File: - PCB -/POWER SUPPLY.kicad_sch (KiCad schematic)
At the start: 5 parts, among them IC1 XT30U-F, U11 LD1086V33-DG, U7 ROB-14450

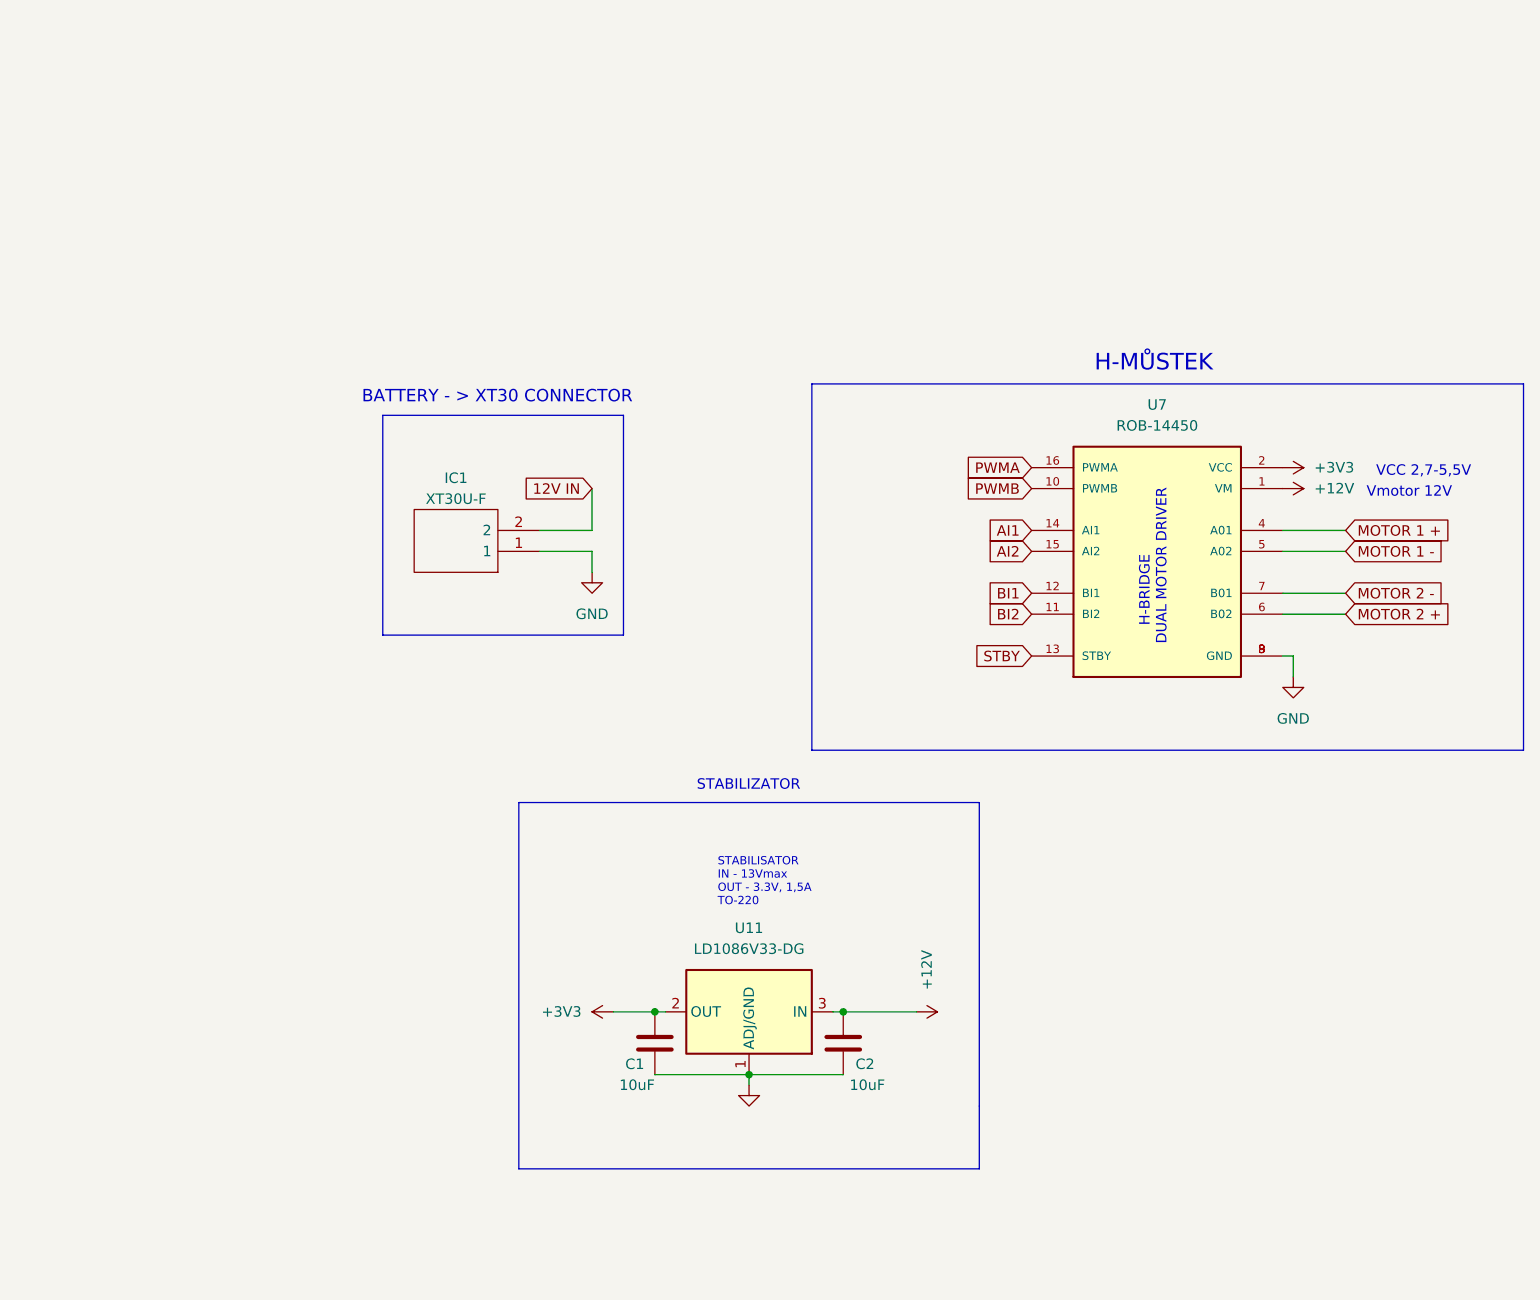
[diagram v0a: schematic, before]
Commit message: PCB - SCH UPDATE (fully labelled and described)
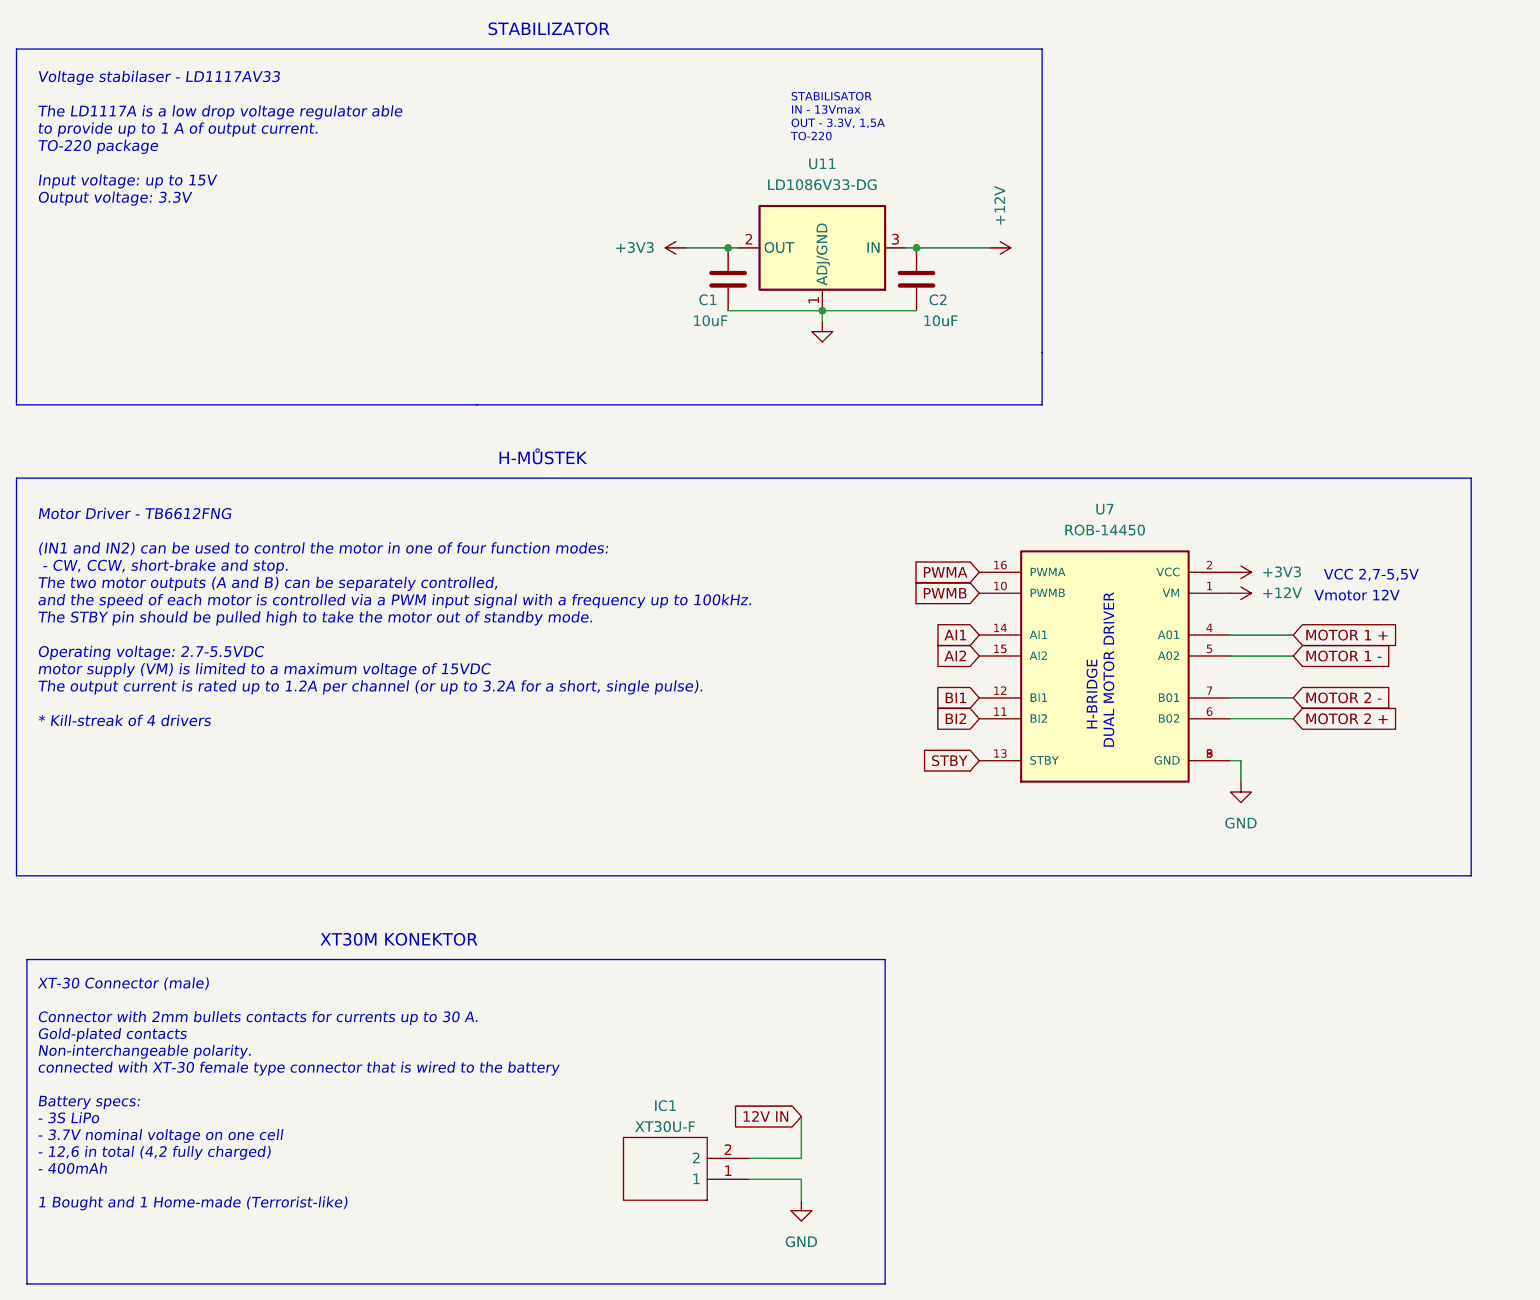
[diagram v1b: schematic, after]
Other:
- note added: "Motor Driver - TB6612FNG (IN1 and IN2) can be used to control the motor in one of four function modes: - CW, CCW, short-brake and stop. The two motor outputs (A and B) can be separately controlled, and the speed of each motor is controlled via a PWM input signal with a frequency up to 100kHz. The STBY pin should be pulled high to take the motor out of standby mode. Operating voltage: 2.7-5.5VDC m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"
- note added: "Voltage stabilaser - LD1117AV33 The LD1117A is a low drop voltage regulator able to provide up to 1 A of output current. TO-220 package Input voltage: up to 15V Output voltage: 3.3V"
- note added: "XT-30 Connector (male) Connector with 2mm bullets contacts for currents up to 30 A. Gold-plated contacts Non-interchangeable polarity. connected with XT-30 female type connector that is wired to the battery Battery specs: - 3S LiPo - 3.7V nominal voltage on one cell - 12,6 in total (4,2 fully charged) - 400mAh 1 Bought and 1 Home-made (Terrorist-like)"
- note added: "XT30M KONEKTOR"
- note removed: "BATTERY - > XT30 CONNECTOR"
- moved on the sheet: C1, C2, IC1, U11, U7

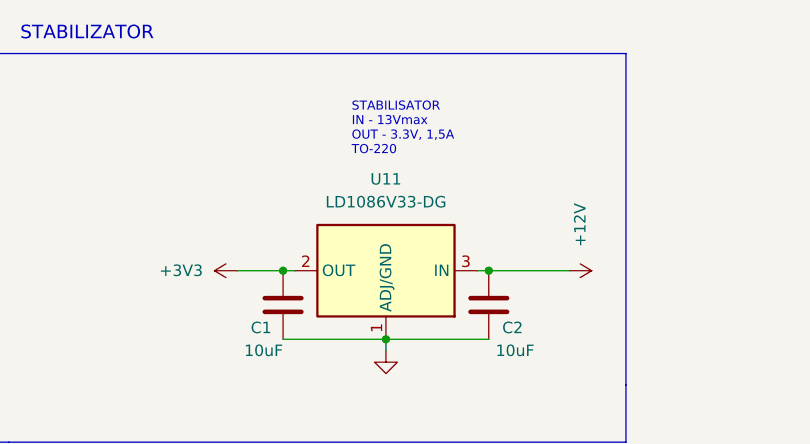
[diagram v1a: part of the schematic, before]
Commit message: PCB - sch and footprint update, QRE1113 3D model.
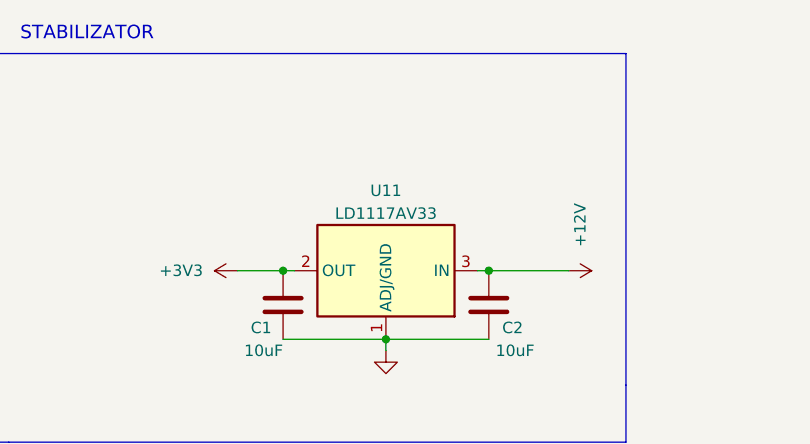
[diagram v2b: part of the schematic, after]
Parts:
- IC1: footprint Connector_AMASS:AMASS_XT30U-M_1x02_P5.0mm_Vertical -> Connector_AMASS:AMASS_XT30UPB-M_1x02_P5.0mm_Vertical
- U11: value LD1086V33-DG -> LD1117AV33
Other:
- note removed: "STABILISATOR IN - 13Vmax OUT - 3.3V, 1,5A TO-220"
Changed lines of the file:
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@@
     (effects (font (size 1.27 1.27)) (justify left bottom))
-  )
-  (text "STABILISATOR\nIN - 13Vmax\nOUT - 3.3V, 1,5A\nTO-220" (at 135.89 33.02 0)
-    (effects (font (size 1 1)) (justify left bottom))
   )
   (text "XT-30 Connector (male)\n\nConnector with 2mm bullets contacts for currents up to 30 A.\nGold-plated contacts\nNon-interchangeable polarity.\nconnected with XT-30 female type connector that is wired to the battery\n\nBattery specs:\n- 3S LiPo\n- 3.7V nominal voltage on one cell\n- 12,6 in total (4,2 fully charged)\n- 400mAh \n\n1 Bought and 1 Home-made (Terrorist-like)"
@@
       (effects (font (size 1.27 1.27)))
     )
-    (property "Footprint" "Connector_AMASS:AMASS_XT30U-M_1x02_P5.0mm_Vertical" (at 114.3 161.29 0)
+    (property "Footprint" "Connector_AMASS:AMASS_XT30UPB-M_1x02_P5.0mm_Vertical" (at 114.3 161.29 0)
       (effects (font (size 1.27 1.27)) (justify left) hide)
     )
@@
   (symbol (lib_id "Regulator_Linear:LD1086V33-DG") (at 139.7 45.72 0) (mirror y) (unit 1)
     (in_bom yes) (on_board yes) (dnp no) (fields_autoplaced)
-    (property "Reference" "U11" (at 139.7 35.56 0)
-      (effects (font (size 1.27 1.27)))
-    )
-    (property "Value" "LD1086V33-DG" (at 139.7 38.1 0)
-      (effects (font (size 1.27 1.27)))
-    )
+    (property "Reference" "U11" (at 139.7 36.83 0)
+      (effects (font (size 1.27 1.27)))
+    )
+    (property "Value" "LD1117AV33" (at 139.7 39.37 0)
+      (effects (font (size 1.27 1.27)))
+    )

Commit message: PCB - Board update
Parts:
- added SW1: SW_SPDT, SWITCH SPDT:SW_100SP1T1B4M2QE, symbol Switch:SW_DPDT_x2
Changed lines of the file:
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@@
+    )
+  )
+  (symbol (lib_id "Switch:SW_DPDT_x2") (at 90.17 100.33 0) (mirror x) (unit 1)
+    (in_bom yes) (on_board yes) (dnp no)
+    (property "Reference" "SW1" (at 90.17 95.25 0)
+      (effects (font (size 1.27 1.27)))
+    )
+    (property "Value" "SW_SPDT" (at 87.63 105.41 0)
+      (effects (font (size 1.27 1.27)))
+    )
+    (property "Footprint" "SWITCH SPDT:SW_100SP1T1B4M2QE" (at 90.17 100.33 0)
+      (effects (font (size 1.27 1.27)) hide)
+    )
+    (property "Datasheet" "~" (at 90.17 100.33 0)
+      (effects (font (size 1.27 1.27)) hide)
+    )
+    (pin "1")
+    (pin "2")
+    (pin "3")
+    (pin "4")
+    (pin "5")
+    (pin "6")
+    (instances
+      (project "sumec"
+        (path "/fc70a1a8-ed7c-4a0f-9b1a-f23293528385/05a35bad-c108-46ad-8f95-76319a60a14f"
+          (reference "SW1") (unit 1)
+        )
+        (path "/fc70a1a8-ed7c-4a0f-9b1a-f23293528385/2febd48c-c6ec-477b-ac64-6fa98a41fff0"
+          (reference "SW1") (unit 1)
+        )
+      )
     )
   )

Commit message: PCB - board update + footprint/3d models export
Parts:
- removed SW1: SW_SPDT, SWITCH SPDT:SW_100SP1T1B4M2QE, symbol Switch:SW_DPDT_x2
- IC?: renamed from IC1; footprint Connector_AMASS:AMASS_XT30UPB-M_1x02_P5.0mm_Vertical -> sumec_library:AMASS_XT30U-M_1x02_P5.0mm_Vertical
- U?: renamed from U7; footprint H-BRIDGE:MODULE_ROB-14450 -> sumec_library:ROB-14450 - TB6612FNG (MOTOR DRIVER)
- renumbered C1 to C?, C2 to C?, U11 to U?

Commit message: PCB sumec THT update
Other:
- company: (none) -> SPŠ NA PROSEKU
- title: (none) -> SUMEC THT
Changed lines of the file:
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@@
 (kicad_sch (version 20230121) (generator eeschema)
   (paper "A4")
+  (title_block
+    (title "SUMEC THT")
+    (company "SPŠ NA PROSEKU")
+  )
   (junction (at 128.27 45.72) (diameter 0) (color 0 0 0 0)
   )
